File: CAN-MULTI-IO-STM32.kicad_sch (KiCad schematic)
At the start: 42 parts, among them J1 H GND L, J2 TERM, J3 UART1, J4 SWLINK, J5 PWR IN, U1 STM32L433RCT3, U2 MCP2562-E-SN

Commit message: schematic and layout refinement
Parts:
- removed CONSW3, CONSW4: Conn_01x05, Connector_PinHeader_2.54mm:PinHeader_1x05_P2.54mm_Horizontal, symbol Connector_Generic:Conn_01x05
- added I2C2: GND SCL SDA 3V3, Connector_PinHeader_2.54mm:PinHeader_1x04_P2.54mm_Horizontal, symbol Connector_Generic:Conn_01x04
- added J6: ONEW, Connector_PinHeader_2.54mm:PinHeader_1x03_P2.54mm_Horizontal, symbol Connector_Generic:Conn_01x03
- added J7: I2C PU EN, Connector_PinHeader_2.54mm:PinHeader_1x02_P2.54mm_Vertical, symbol Connector_Generic:Conn_01x02
- added RPU1, RPU2, RPU3: 4K7, Resistor_SMD:R_0603_1608Metric_Pad0.98x0.95mm_HandSolder, symbol Device:R_US
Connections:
- net +3.3V: now also I2C2.4 (Pin_4), J6.3 (Pin_3), J7.2 (Pin_2), RPU3.2
- net GND: now also I2C2.1 (Pin_1), J6.1 (Pin_1), RPU3.1
- net ONEW: now reaches U1.24 (PC4)
- net ONEW: now also J6.2 (Pin_2)
- net I2C2_SCL: now reaches U1.29 (PB10)
- net I2C2_SCL: now also I2C2.2 (Pin_2), RPU2.1
- net I2C2_SDA: now reaches U1.30 (PB11)
- net I2C2_SDA: now also I2C2.3 (Pin_3), RPU1.1
- net ADC1_IN10: no longer names the net of U1.21 (PA5)
- net ADC1_IN11: no longer names the net of U1.22 (PA6)
- net ADC1_IN12: no longer names the net of U1.23 (PA7)
- net ADC1_IN8: no longer names the net of U1.17 (PA3)
- net ADC1_IN9: no longer names the net of U1.20 (PA4)
- net CTL2: no longer names the net of U1.61 (PB8)
- net CTL3: no longer names the net of U1.57 (PB5)
- net CTL4: no longer names the net of U1.52 (PC11)
- net DEN2: no longer names the net of U1.62 (PB9)
- net DEN3: no longer names the net of U1.54 (PD2)
- net DEN4: no longer names the net of U1.50 (PA15)
- new net: J7.1 (Pin_1), RPU1.2, RPU2.2

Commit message: final tweaks
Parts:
- I2C2: value GND SCL SDA 3V3 -> G SCL SDA 3V
- ONEWIRE1: renamed from J6; value ONEW -> G OW 3V
- renumbered ANA_IN1 to ADIO1, ANA_IN2 to ADIO2
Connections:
- net GND: no longer RPU3.1
- net ONEW: now also RPU3.1
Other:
- moved on the sheet: RPU3
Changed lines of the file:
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@@
 	)
 	(junction
-		(at 101.6 176.53)
-		(diameter 0)
-		(color 0 0 0 0)
-	)
-	(junction
 		(at 39.37 144.78)
 		(diameter 0)
@@
 	)
 	(junction
-		(at 101.6 165.1)
-		(diameter 0)
-		(color 0 0 0 0)
-	)
-	(junction
 		(at 68.58 25.4)
 		(diameter 0)
@@
 	)
 	(junction
+		(at 101.6 160.02)
+		(diameter 0)
+		(color 0 0 0 0)
+	)
+	(junction
 		(at 139.7 45.72)
 		(diameter 0)
@@
 	(wire
 		(pts
-			(xy 107.95 165.1) (xy 107.95 167.64)
+			(xy 107.95 160.02) (xy 107.95 161.29)
 		)
 		(stroke
@@
 	(wire
 		(pts
+			(xy 101.6 160.02) (xy 101.6 168.91)
+		)
+		(stroke
+			(width 0)
+			(type default)
+		)
+	)
+	(wire
+		(pts
 			(xy 111.76 88.9) (xy 111.76 99.06)
 		)
@@
 	(wire
 		(pts
-			(xy 101.6 165.1) (xy 101.6 161.29)
-		)
-		(stroke
-			(width 0)
-			(type default)
-		)
-	)
-	(wire
-		(pts
 			(xy 73.66 22.86) (xy 73.66 48.26)
 		)
@@
 	(wire
 		(pts
-			(xy 101.6 176.53) (xy 107.95 176.53)
-		)
-		(stroke
-			(width 0)
-			(type default)
-		)
-	)
-	(wire
-		(pts
 			(xy 34.29 152.4) (xy 39.37 152.4)
 		)
@@
 	(wire
 		(pts
-			(xy 101.6 176.53) (xy 101.6 177.8)
-		)
-		(stroke
-			(width 0)
-			(type default)
-		)
-	)
-	(wire
-		(pts
-			(xy 101.6 168.91) (xy 101.6 165.1)
+			(xy 101.6 173.99) (xy 101.6 177.8)
 		)
 		(stroke
@@
 	(wire
 		(pts
-			(xy 93.98 171.45) (xy 99.06 171.45)
+			(xy 93.98 171.45) (xy 107.95 171.45)
 		)
 		(stroke
@@
 	(wire
 		(pts
-			(xy 107.95 176.53) (xy 107.95 175.26)
+			(xy 208.28 123.19) (xy 208.28 124.46)
 		)
 		(stroke
@@
 	(wire
 		(pts
-			(xy 208.28 123.19) (xy 208.28 124.46)
+			(xy 256.54 68.58) (xy 261.62 68.58)
 		)
 		(stroke
@@
 	(wire
 		(pts
-			(xy 256.54 68.58) (xy 261.62 68.58)
+			(xy 74.93 111.76) (xy 74.93 106.68)
 		)
 		(stroke
@@
 	(wire
 		(pts
-			(xy 74.93 111.76) (xy 74.93 106.68)
+			(xy 104.14 111.76) (xy 107.95 111.76)
 		)
 		(stroke
@@
 	(wire
 		(pts
-			(xy 104.14 111.76) (xy 107.95 111.76)
+			(xy 43.18 41.91) (xy 43.18 48.26)
 		)
 		(stroke
@@
 	(wire
 		(pts
-			(xy 43.18 41.91) (xy 43.18 48.26)
+			(xy 101.6 160.02) (xy 101.6 157.48)
 		)
 		(stroke
@@
 	(wire
 		(pts
-			(xy 101.6 173.99) (xy 101.6 176.53)
-		)
-		(stroke
-			(width 0)
-			(type default)
-		)
-	)
-	(wire
-		(pts
 			(xy 39.37 144.78) (xy 54.61 144.78)
 		)
@@
 	(wire
 		(pts
+			(xy 107.95 171.45) (xy 107.95 168.91)
+		)
+		(stroke
+			(width 0)
+			(type default)
+		)
+	)
+	(wire
+		(pts
 			(xy 261.62 119.38) (xy 261.62 109.22)
 		)
@@
 	(wire
 		(pts
-			(xy 101.6 165.1) (xy 107.95 165.1)
+			(xy 101.6 160.02) (xy 107.95 160.02)
 		)
 		(stroke
@@
 		)
 	)
-	(label "ONEW"
-		(at 99.06 171.45 0)
-		(effects
-			(font
-				(size 1.27 1.27)
-			)
-			(justify left bottom)
-		)
-	)
 	(label "ADC1_IN1"
 		(at 119.38 81.28 180)
@@
 		)
 	)
-	(label "ONEw"
-		(at 99.06 171.45 0)
-		(effects
-			(font
-				(size 1.27 1.27)
-			)
-			(justify left bottom)
-		)
-	)
 	(label "CANL"
 		(at 252.73 106.68 0)
@@
 		)
 	)
+	(label "ONEW"
+		(at 97.79 171.45 0)
+		(effects
+			(font
+				(size 1.27 1.27)
+			)
+			(justify left bottom)
+		)
+	)
 	(label "SWO"
 		(at 163.83 111.76 0)
@@
 		(dnp no)
 		(fields_autoplaced yes)
-		(property "Reference" "ANA_IN1"
+		(property "Reference" "ADIO1"
 			(at 29.21 107.95 0)
 			(effects
@@
 			(project ""
 				(path "/807782eb-8307-4922-8e5a-50da44718f8e"
-					(reference "ANA_IN1")
+					(reference "ADIO1")
 					(unit 1)
 				)
@@
 	(symbol
 		(lib_id "Device:R_US")
-		(at 107.95 171.45 180)
+		(at 107.95 165.1 180)
 		(unit 1)
 		(exclude_from_sim no)
@@
 		(fields_autoplaced yes)
 		(property "Reference" "RPU3"
-			(at 110.49 170.1799 0)
+			(at 110.49 163.8299 0)
 			(effects
 				(font
@@
 		)
 		(property "Value" "4K7"
-			(at 110.49 172.7199 0)
+			(at 110.49 166.3699 0)
 			(effects
 				(font
@@
 		)
 		(property "Footprint" "Resistor_SMD:R_0603_1608Metric_Pad0.98x0.95mm_HandSolder"
-			(at 106.934 171.196 90)
+			(at 106.934 164.846 90)
 			(effects
 				(font
@@
 		)
 		(property "Datasheet" "~"
-			(at 107.95 171.45 0)
+			(at 107.95 165.1 0)
 			(effects
 				(font
@@
 		)
 		(property "Description" "Resistor, US symbol"
-			(at 107.95 171.45 0)
+			(at 107.95 165.1 0)
 			(effects
 				(font
@@
 		(dnp no)
 		(fields_autoplaced yes)
-		(property "Reference" "J6"
+		(property "Reference" "ONEWIRE1"
 			(at 88.9 162.56 0)
 			(effects
@@
 			)
 		)
-		(property "Value" "ONEW"
+		(property "Value" "G OW 3V"
 			(at 88.9 165.1 0)
 			(effects
@@
 			(project ""
 				(path "/807782eb-8307-4922-8e5a-50da44718f8e"
-					(reference "J6")
+					(reference "ONEWIRE1")
 					(unit 1)
 				)
@@
 		(dnp no)
 		(fields_autoplaced yes)
-		(property "Reference" "ANA_IN2"
+		(property "Reference" "ADIO2"
 			(at 64.77 107.95 0)
 			(effects
@@
 			(project ""
 				(path "/807782eb-8307-4922-8e5a-50da44718f8e"
-					(reference "ANA_IN2")
+					(reference "ADIO2")
 					(unit 1)
 				)
@@
 			)
 		)
-		(property "Value" "GND SCL SDA 3V3"
+		(property "Value" "G SCL SDA 3V"
 			(at 29.21 148.59 0)
 			(effects
@@
 	(symbol
 		(lib_id "power:+3.3V")
-		(at 101.6 161.29 0)
+		(at 101.6 157.48 0)
 		(unit 1)
 		(exclude_from_sim no)
@@
 		(fields_autoplaced yes)
 		(property "Reference" "#PWR031"
-			(at 101.6 165.1 0)
+			(at 101.6 161.29 0)
 			(effects
 				(font
@@
 		)
 		(property "Value" "+3.3V"
-			(at 101.6 156.21 0)
+			(at 101.6 152.4 0)
 			(effects
 				(font
@@
 		)
 		(property "Footprint" ""
-			(at 101.6 161.29 0)
+			(at 101.6 157.48 0)
 			(effects
 				(font
@@
 		)
 		(property "Datasheet" ""
-			(at 101.6 161.29 0)
+			(at 101.6 157.48 0)
 			(effects
 				(font
@@
 		)
 		(property "Description" "Power symbol creates a global label with name \"+3.3V\""
-			(at 101.6 161.29 0)
+			(at 101.6 157.48 0)
 			(effects
 				(font

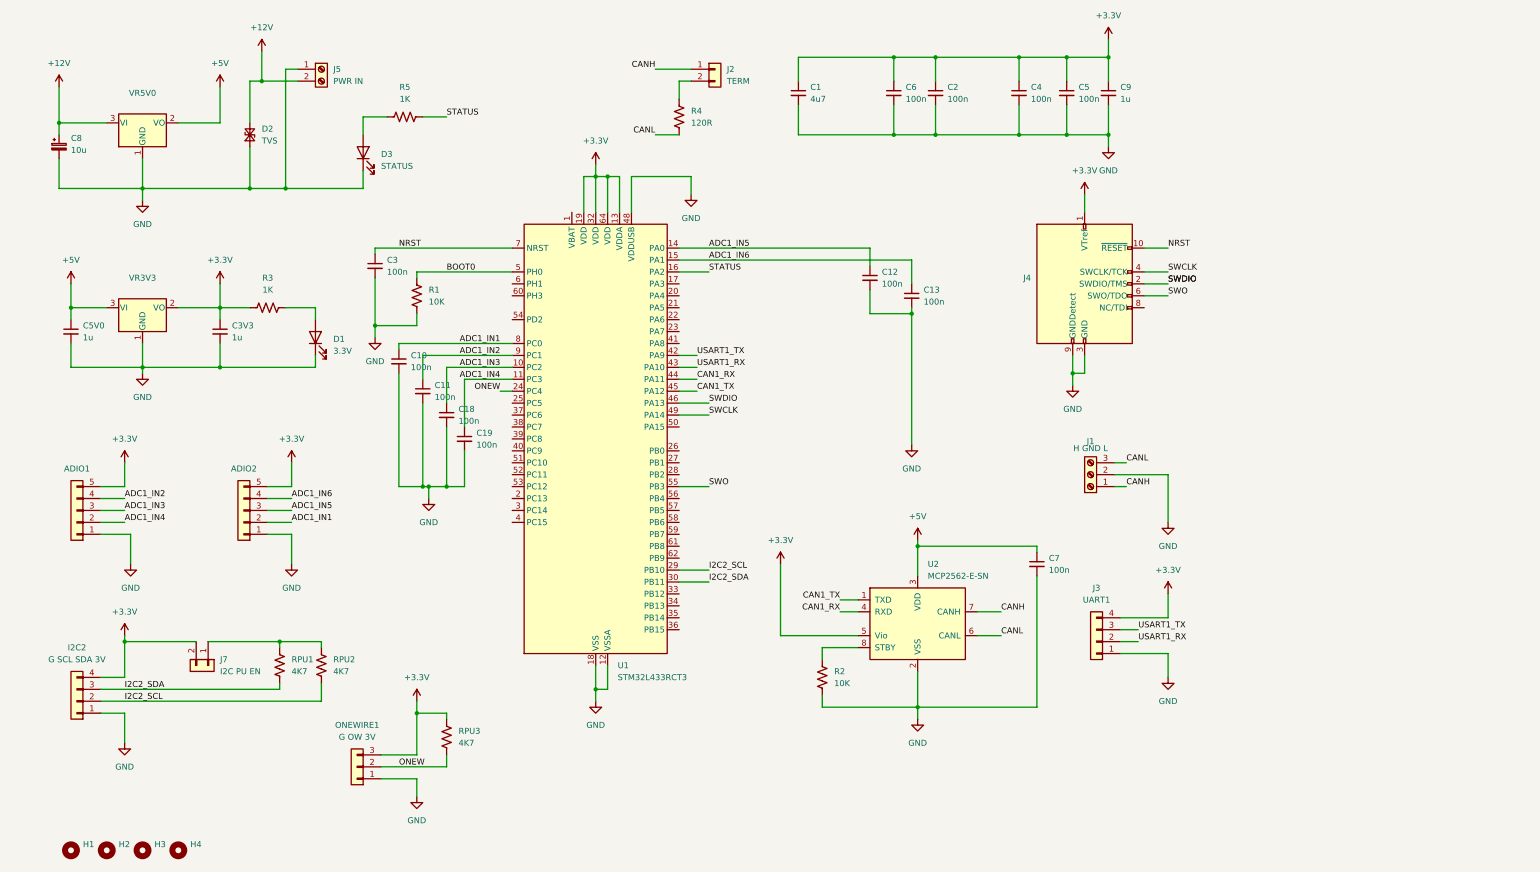
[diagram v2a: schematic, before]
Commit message: major rework to include SMPS and better analog input configuration
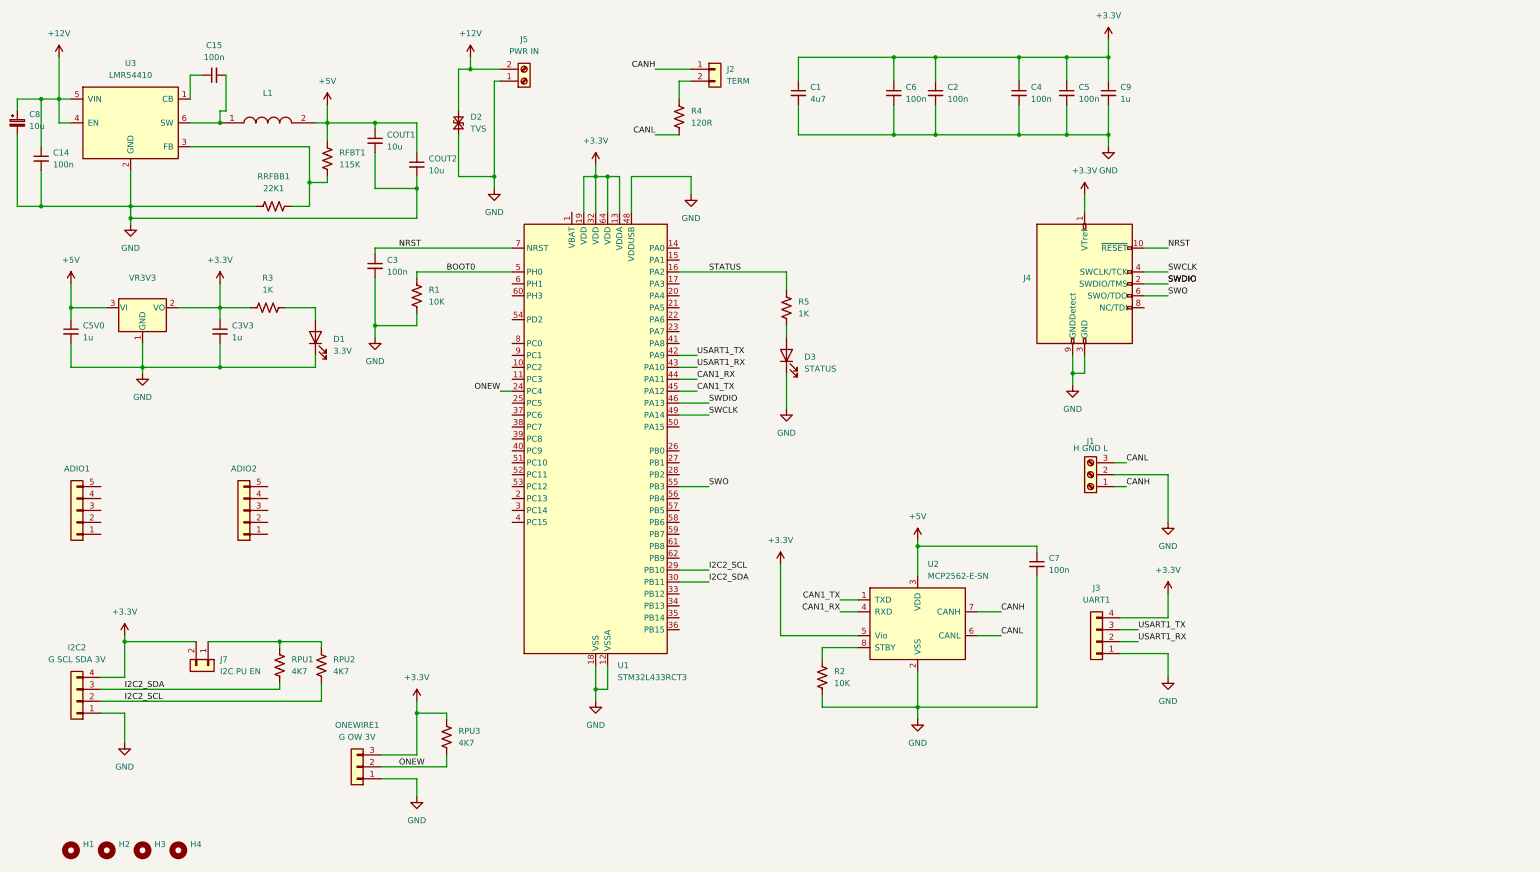
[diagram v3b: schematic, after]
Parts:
- removed C10, C11, C12, C13, C18, C19: 100n, Capacitor_SMD:C_0603_1608Metric_Pad1.08x0.95mm_HandSolder, symbol Device:C_Small
- removed VR5V0: TLV1117-50, Package_TO_SOT_SMD:SOT-223-3_TabPin2, symbol Regulator_Linear:TLV1117-50
- added C14, C15: 100n, Capacitor_SMD:C_0603_1608Metric_Pad1.08x0.95mm_HandSolder, symbol Device:C_Small
- added COUT1, COUT2: 10u, Capacitor_SMD:C_0805_2012Metric_Pad1.18x1.45mm_HandSolder, symbol Device:C_Small
- added L1: VLS5045EX-100M-H, VLS5045EX330M, symbol SamacSys_Parts:VLS5045EX-100M-H
- added RFBT1: 115K, Resistor_SMD:R_0603_1608Metric_Pad0.98x0.95mm_HandSolder, symbol Device:R_US
- added RRFBB1: 22K1, Resistor_SMD:R_0603_1608Metric_Pad0.98x0.95mm_HandSolder, symbol Device:R_US
- added U3: LMR54410, Package_TO_SOT_SMD:SOT-23-6, symbol Regulator_Switching:LMR50410
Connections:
- net +12V: now also C14.1, U3.4 (EN), U3.5 (VIN)
- net +3.3V: no longer ADIO1.5 (Pin_5), ADIO2.5 (Pin_5)
- net +5V: now also COUT1.1, COUT2.1, L1.2, RFBT1.1
- net GND: now also C14.2, COUT1.2, COUT2.2, RRFBB1.1, U3.2 (GND); no longer ADIO1.1 (Pin_1), ADIO2.1 (Pin_1)
- net ADC1_IN1: no longer names the net of ADIO2.2 (Pin_2)
- net ADC1_IN1: no longer U1.8 (PC0)
- net ADC1_IN2: no longer names the net of ADIO1.4 (Pin_4)
- net ADC1_IN2: no longer U1.9 (PC1)
- net ADC1_IN3: no longer names the net of ADIO1.3 (Pin_3)
- net ADC1_IN3: no longer U1.10 (PC2)
- net ADC1_IN4: no longer names the net of ADIO1.2 (Pin_2)
- net ADC1_IN4: no longer U1.11 (PC3)
- net ADC1_IN5: no longer names the net of ADIO2.3 (Pin_3)
- net ADC1_IN5: no longer U1.14 (PA0)
- net ADC1_IN6: no longer names the net of ADIO2.4 (Pin_4)
- net ADC1_IN6: no longer U1.15 (PA1)
- new net: C15.1, U3.1 (CB)
- new net: C15.2, L1.1, U3.6 (SW)
- new net: RFBT1.2, RRFBB1.2, U3.3 (FB)
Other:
- moved on the sheet: C8, D2, D3, J5, R5

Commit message: optimized some connectors, switched to SMPS for 5v supply rail
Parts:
- removed C8: 10u, Capacitor_THT:CP_Radial_D5.0mm_P2.50mm, symbol Device:C_Polarized_Small
- removed J4: SWLINK, Connector_PinHeader_2.54mm:PinHeader_2x05_P2.54mm_Horizontal, symbol Connector:Conn_ARM_JTAG_SWD_10
- added CIN1: 10u, Capacitor_SMD:C_1210_3225Metric_Pad1.33x2.70mm_HandSolder, symbol Device:C_Small
- added SWD: G CK D V R, PCM_SparkFun-Connector:1x05_P2.54mm_Locking, symbol Connector_Generic:Conn_01x05
- D1, D3: footprint LED_THT:LED_D5.0mm_Clear -> LED_SMD:LED_0805_2012Metric_Pad1.15x1.40mm_HandSolder
- J3: footprint Connector_PinHeader_2.54mm:PinHeader_1x04_P2.54mm_Horizontal -> PCM_SparkFun-Connector:1x04_P2.54mm_Locking
- renumbered C14 to CIN2
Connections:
- net +12V: now also CIN1.1
- net +3.3V: now also SWD.4 (Pin_4)
- net GND: now also CIN1.2, SWD.1 (Pin_1)
- net NRST: now also SWD.5 (Pin_5)
- net SWCLK: now also SWD.2 (Pin_2)
- net SWDIO: now also SWD.3 (Pin_3)
- net CB: now reaches C15.1, U3.1 (CB)
- net SW: now reaches C15.2, L1.1, U3.6 (SW)

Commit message: added i2c adc and gpio chips to isolate the mcu, lots of layout work
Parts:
- removed ADIO1: G A4 A3 A2 3V, Connector_PinHeader_2.54mm:PinHeader_1x05_P2.54mm_Horizontal, symbol Connector_Generic:Conn_01x05
- removed ADIO2: G A1 A5 A6 3V, Connector_PinHeader_2.54mm:PinHeader_1x05_P2.54mm_Horizontal, symbol Connector_Generic:Conn_01x05
- added ANA_IN1, ANA_IN2: Conn_01x06, TerminalBlock_TE-Connectivity:TerminalBlock_TE_282834-6_1x06_P2.54mm_Horizontal, symbol Connector_Generic:Conn_01x06
- added CTCA1: 100n, Capacitor_SMD:C_0603_1608Metric_Pad1.08x0.95mm_HandSolder, symbol Device:C_Small
- added RPU4, RPU5: 4K7, Resistor_SMD:R_0603_1608Metric_Pad0.98x0.95mm_HandSolder, symbol Device:R_US
- added RPU6, RPU7: 10K, Resistor_SMD:R_0603_1608Metric_Pad0.98x0.95mm_HandSolder, symbol Device:R_US
- added U4, U5: ADS1015IDGS, Package_SO:TSSOP-10_3x3mm_P0.5mm, symbol Analog_ADC:ADS1015IDGS
- added U6: TCA9511, Package_SO:VSSOP-8_3x3mm_P0.65mm, symbol SamacSys_Parts:TCA9511ADGKR
- D3: value STATUS -> STAT
- J3: value UART1 -> USART1
- RPU1, RPU2: value 4K7 -> 10K
- SWD1: renamed from SWD; value G CK D V R -> STLINK
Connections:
- net +3.3V: now also RPU1.2, RPU2.2, ANA_IN1.6 (Pin_6), ANA_IN2.6 (Pin_6), CTCA1.1, RPU4.2, RPU5.2, RPU6.2, RPU7.2, U4.8 (VDD), U5.8 (VDD), U6.8 (VCC)
- net GND: now also ANA_IN1.1 (Pin_1), ANA_IN2.1 (Pin_1), CTCA1.2, U4.3 (GND), U5.3 (GND), U6.4 (GND)
- net I2C2_SCL: now also U6.3 (SCLIN); no longer I2C2.2 (Pin_2)
- net I2C2_SDA: now also U6.6 (SDAIN); no longer I2C2.3 (Pin_3)
- net I2C1_SCL: now reaches U1.61 (PB8)
- net I2C1_SCL: now also RPU7.1, U4.1 (ADDR), U4.10 (SCL), U5.10 (SCL)
- net I2C1_SDA: now reaches U1.62 (PB9)
- net I2C1_SDA: now also RPU6.1, U4.9 (SDA), U5.1 (ADDR), U5.9 (SDA)
- net SWO: no longer names the net of U1.55 (PB3)
- new net: ANA_IN1.5 (Pin_5), U4.4 (AIN0)
- new net: ANA_IN1.4 (Pin_4), U4.5 (AIN1)
- new net: ANA_IN1.3 (Pin_3), U4.6 (AIN2)
- new net: ANA_IN1.2 (Pin_2), U4.7 (AIN3)
- new net: ANA_IN2.2 (Pin_2), U5.7 (AIN3)
- new net: ANA_IN2.3 (Pin_3), U5.6 (AIN2)
- new net: ANA_IN2.4 (Pin_4), U5.5 (AIN1)
- new net: ANA_IN2.5 (Pin_5), U5.4 (AIN0)
- new net SCLOUT: I2C2.2 (Pin_2), RPU5.1, U6.2 (SCLOUT)
- new net SDAOUT: I2C2.3 (Pin_3), RPU4.1, U6.7 (SDAOUT)
- now unconnected: J7.1 (Pin_1)
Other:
- moved on the sheet: C2, C4, C5, C6, C9, I2C2, J1, J3, RPU1, RPU2, SWD1

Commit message: lots of progress, lots to do
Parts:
- removed J7: I2C PU EN, Connector_PinHeader_2.54mm:PinHeader_1x02_P2.54mm_Vertical, symbol Connector_Generic:Conn_01x02
- removed U5: ADS1015IDGS, Package_SO:TSSOP-10_3x3mm_P0.5mm, symbol Analog_ADC:ADS1015IDGS
- added CAIN0, CAIN1, CAIN2, CAIN3, CTCA2, CTCA3: 100n, Capacitor_SMD:C_0603_1608Metric_Pad1.08x0.95mm_HandSolder, symbol Device:C_Small
- added R6: 10K, Resistor_SMD:R_0603_1608Metric_Pad0.98x0.95mm_HandSolder, symbol Device:R_US
- added R7, R8: 10K, Resistor_SMD:R_0603_1608Metric_Pad0.98x0.95mm_HandSolder, symbol Device:R_Small_US
- added U5: PCA9537, Package_SO:TSSOP-10_3x3mm_P0.5mm, symbol Interface_Expansion:PCA9537
- renumbered ANA_IN2 to GPIO_CON1, I2C2 to I2CEXT1
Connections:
- net +3.3V: now also ANA_IN1.1 (Pin_1), CTCA2.1, CTCA3.1, R6.1, R8.1, U5.10 (VDD); no longer ANA_IN1.6 (Pin_6)
- net GND: now also ANA_IN1.6 (Pin_6), U4.1 (ADDR), CAIN0.2, CAIN1.2, CAIN2.2, CAIN3.2, CTCA2.2, CTCA3.2, R7.2, U5.5 (VSS); no longer ANA_IN1.1 (Pin_1)
- net I2C1_SCL: now also U5.8 (SCL); no longer U4.1 (ADDR)
- net I2C1_SDA: now also U5.9 (SDA)
- net USART1_RX: now also J3.3 (Pin_3); no longer J3.2 (Pin_2)
- net USART1_TX: now also J3.2 (Pin_2); no longer J3.3 (Pin_3)
- net AIN0: now reaches U4.4 (AIN0)
- net AIN0: now also ANA_IN1.2 (Pin_2), CAIN0.1; no longer ANA_IN1.5 (Pin_5)
- net AIN1: now reaches U4.5 (AIN1)
- net AIN1: now also ANA_IN1.3 (Pin_3), CAIN1.1; no longer ANA_IN1.4 (Pin_4)
- net AIN2: now reaches U4.6 (AIN2)
- net AIN2: now also ANA_IN1.4 (Pin_4), CAIN2.1; no longer ANA_IN1.3 (Pin_3)
- net AIN3: now reaches U4.7 (AIN3)
- net AIN3: now also ANA_IN1.5 (Pin_5), CAIN3.1; no longer ANA_IN1.2 (Pin_2)
- net at GPIO_CON1.2 (Pin_2): now also U5.4 (IO3)
- net at GPIO_CON1.3 (Pin_3): now also U5.3 (IO2)
- net at GPIO_CON1.4 (Pin_4): now also U5.2 (IO1)
- net at GPIO_CON1.5 (Pin_5): now also U5.1 (IO0)
- net TCA_EN: now reaches U6.1 (EN)
- net TCA_EN: now also U1.52 (PC11), R7.1
- net TCA_RDY: now reaches U6.5 (READY)
- net TCA_RDY: now also U1.51 (PC10), R8.2
- new net: R6.2, U5.6 (~{RESET})
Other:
- moved on the sheet: ANA_IN1, J2
